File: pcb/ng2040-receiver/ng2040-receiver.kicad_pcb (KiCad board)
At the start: 2 copper layers, 40 x 37 mm, 16 parts, among them J1 DB15_F, SW1 OPTS, U1 RP2040-Zero, U2 NRF24L01_Breakout

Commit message: WIP moving radio to top of receiver
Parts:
- removed C1: 0.1uF, Capacitor_SMD:C_0805_2012Metric_Pad1.18x1.45mm_HandSolder
- added C3: 0.1uF, Capacitor_SMD:C_0805_2012Metric_Pad1.18x1.45mm_HandSolder, F.Cu at (90.6, 73.6)
- added C4: 10uF, Capacitor_SMD:C_0805_2012Metric_Pad1.18x1.45mm_HandSolder, F.Cu at (88.4, 73.6)
- C2: value 0.1uF -> 10nF; moved to F.Cu
- R1, R10, R2, R3, R4, R5, R6, R7, R8, R9, U1: moved to B.Cu
- U2: moved to F.Cu
- moved U1 19.5 mm to (104.6, 57.7), turned to -90 degrees
- moved C2 19.0 mm to (92.8, 73.6), turned to 90 degrees
- moved U2 13.3 mm to (100.0, 66.8)
- moved R9 10.3 mm to (102.2, 81.0)
- moved SW1 7.29 mm to (115.4, 70.8), turned to -90 degrees
- moved R8 7.01 mm to (99.7, 81.0)
- moved R7 6.62 mm to (97.1, 81.0)
- moved R6 6.23 mm to (94.6, 81.0)
- moved R5 5.84 mm to (92.0, 81.0)
- moved R4 5.45 mm to (89.4, 81.0)
- moved R3 5.06 mm to (86.9, 81.0)
- moved R10 4.83 mm to (104.8, 81.0)
- moved R2 4.68 mm to (84.3, 81.0)
- moved R1 4.29 mm to (81.8, 81.0)
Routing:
- net /STA: track 40.6 -> 12.3 mm
- net /SET_PLAYER: track 25.5 -> 0.00 mm, vias 1 -> 0
- net /SET_POWER: track 23.1 -> 0.00 mm, vias 1 -> 0
- net /BD: track 34.0 -> 11.5 mm
- net /BC: track 34.7 -> 13.9 mm
- net /DU: track 36.5 -> 16.8 mm
- net /BB: track 30.4 -> 10.9 mm
- net /BA: track 32.9 -> 14.2 mm
- net /SEL: track 31.2 -> 13.5 mm
- net /DR: track 29.4 -> 12.0 mm
- net GND: track 16.6 -> 0.00 mm, vias 33 -> 10
- net /DL: track 32.6 -> 16.5 mm
- net /MOSI: track 32.8 -> 17.8 mm, vias 0 -> 1
- net /VCC: track 17.4 -> 32.0 mm, vias 0 -> 1
- net /DD: track 30.3 -> 15.7 mm
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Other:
- board text added: "TODO put NRF on top"

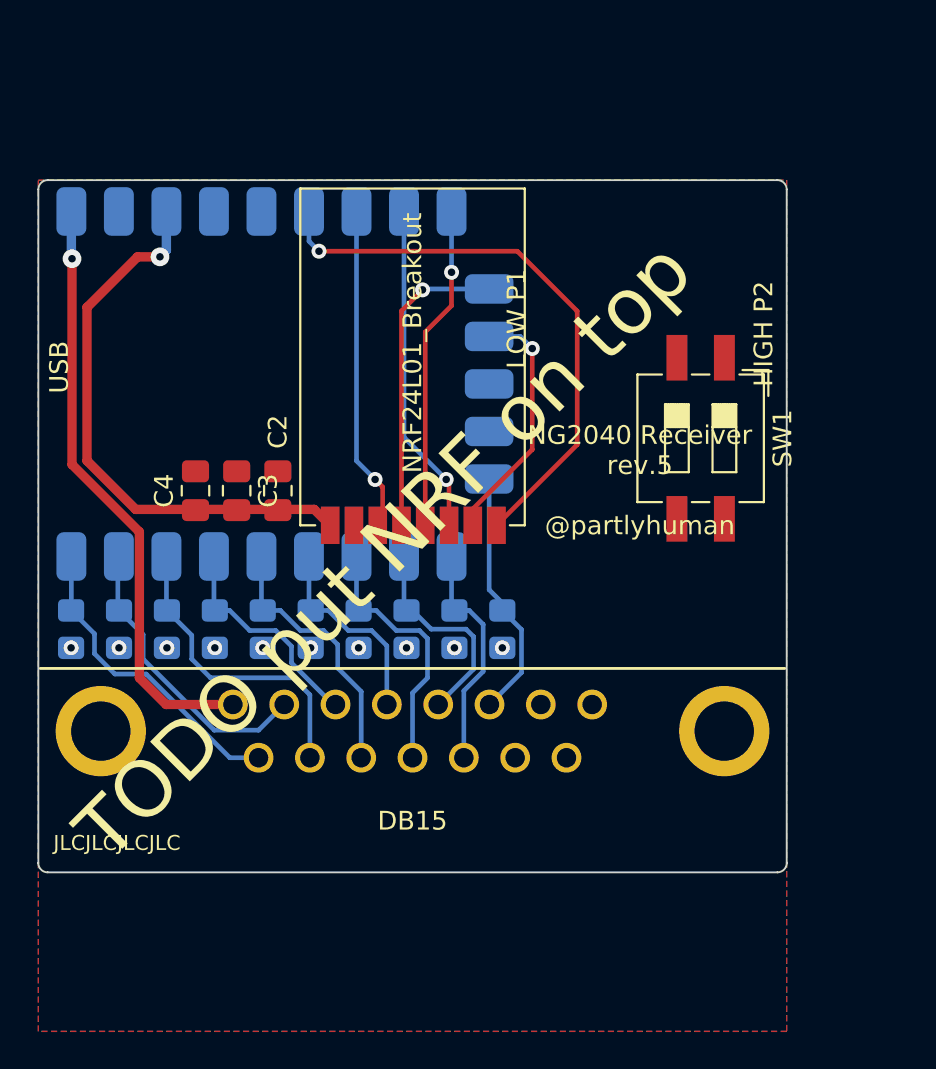
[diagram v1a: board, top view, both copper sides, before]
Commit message: trimming receiver board
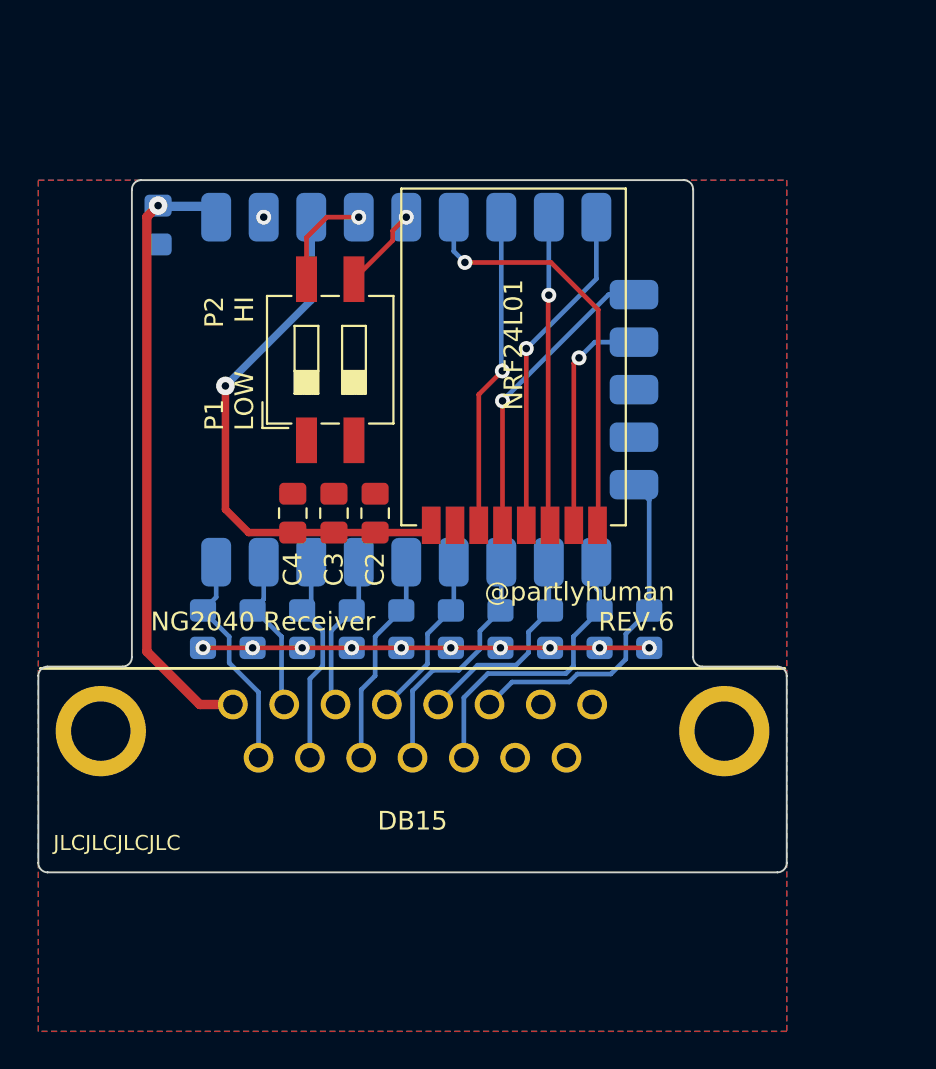
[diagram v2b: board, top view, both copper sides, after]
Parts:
- added C1: 0.1uF, Capacitor_SMD:C_0805_2012Metric_Pad1.18x1.45mm_HandSolder, B.Cu at (86.4, 59.4)
- U2: value NRF24L01_Breakout -> NRF24L01
- moved SW1 20.2 mm to (95.6, 66.6), turned to 90 degrees
- moved R10 7.85 mm to (112.7, 81.0)
- moved R9 7.76 mm to (110.0, 81.0)
- moved U1 7.75 mm to (112.4, 58.0)
- moved R8 7.67 mm to (107.3, 81.0)
- moved R7 7.58 mm to (104.7, 81.0)
- moved R6 7.49 mm to (102.0, 81.0)
- moved R5 7.41 mm to (99.4, 81.0)
- moved R4 7.32 mm to (96.8, 81.0)
- moved R3 7.23 mm to (94.1, 81.0)
- moved R2 7.14 mm to (91.5, 81.0)
- moved R1 7.05 mm to (88.8, 81.0)
- moved U2 5.40 mm to (105.4, 66.8)
- moved C2 5.34 mm to (98.0, 74.8)
- moved C3 5.34 mm to (95.8, 74.8)
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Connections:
- SW1 pad 1: /SET_PLAYER -> GND
- SW1 pad 2: /SET_POWER -> GND
- SW1 pad 3: GND -> /SET_POWER
- SW1 pad 4: GND -> /SET_PLAYER
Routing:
- net GND: track 0.00 -> 23.9 mm, vias 10 -> 11
- net /IRQ: track 30.7 -> 22.4 mm
- net /DD: track 15.7 -> 8.64 mm
- net /SET_PLAYER: track 0.00 -> 5.47 mm, vias 0 -> 1
- net /DL: track 16.5 -> 11.4 mm
- net /SEL: track 13.5 -> 18.5 mm
- net /DU: track 16.8 -> 12.0 mm
- net /SET_POWER: track 0.00 -> 4.47 mm, vias 0 -> 1
- net /DR: track 12.0 -> 8.32 mm
- net /STA: track 12.3 -> 16.0 mm
- net /BA: track 14.2 -> 11.5 mm
- net /BB: track 10.9 -> 9.09 mm
- net /MOSI: track 17.8 -> 16.5 mm
- net /VCC: track 32.0 -> 33.2 mm
- net /3V3: track 30.2 -> 29.2 mm
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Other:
- outline, holes or cut-outs redrawn
- board text added: "${COMPANY} REV.${REVISION}"
- board text added: "${TITLE}"
- board text added: "P1 LOW"
- board text added: "P2 HI"
- board text removed: "${TITLE} rev.${REVISION} ${COMPANY}"
- board text removed: "HIGH P2"
- board text removed: "LOW P1"
- board text removed: "TODO put NRF on top"

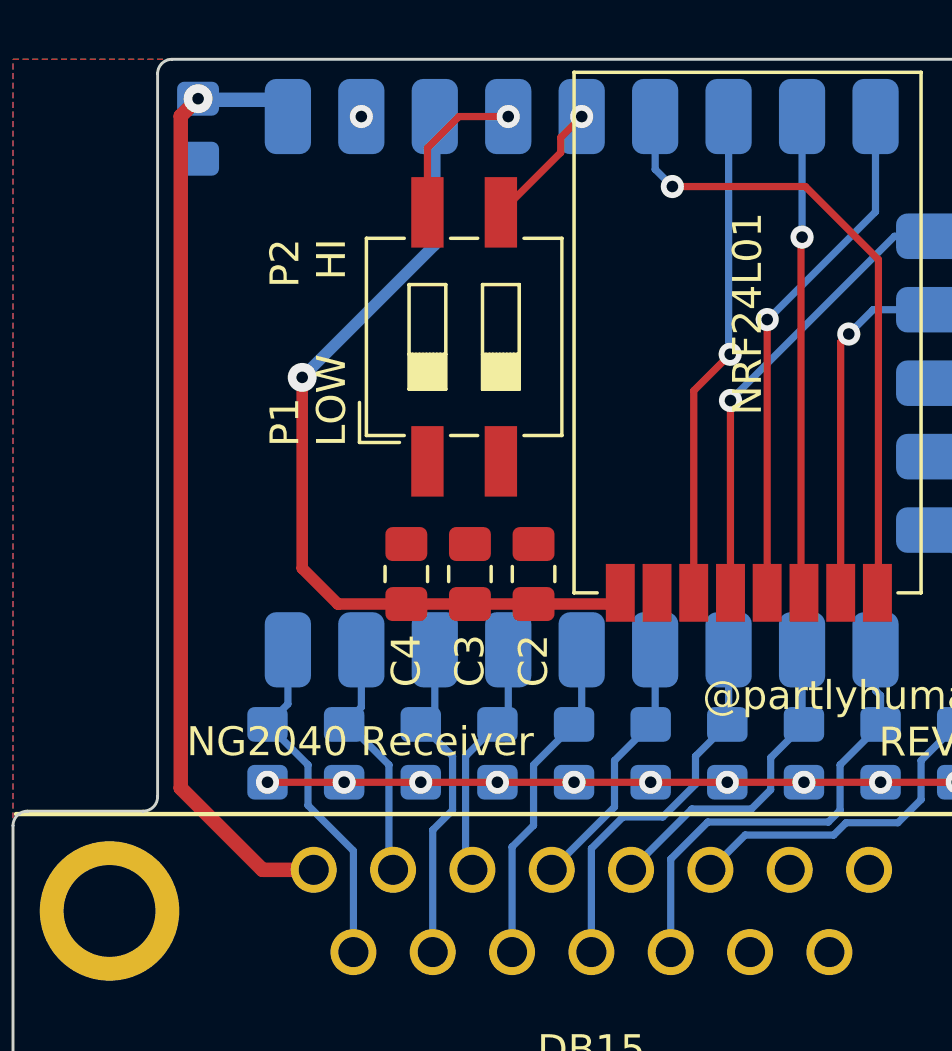
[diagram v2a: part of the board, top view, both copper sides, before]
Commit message: Rerouting
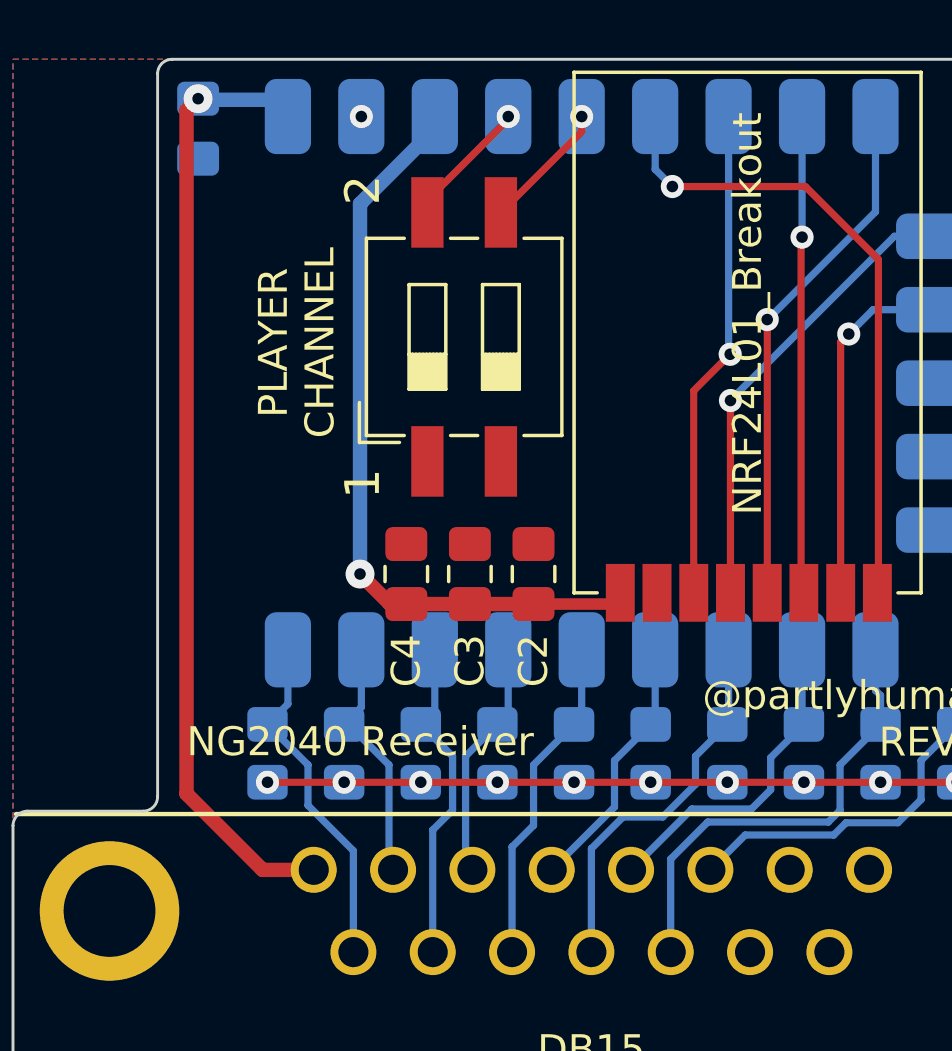
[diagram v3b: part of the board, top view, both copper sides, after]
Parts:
- U2: value NRF24L01 -> NRF24L01_Breakout
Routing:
- net /3V3: track 29.2 -> 26.5 mm
- net /SET_PLAYER: track 5.47 -> 4.47 mm
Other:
- board text added: "1"
- board text added: "2"
- board text added: "PLAYER CHANNEL"
- board text removed: "P1 LOW"
- board text removed: "P2 HI"
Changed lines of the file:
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@@
 			)
 		)
-		(property "Value" "NRF24L01"
+		(property "Value" "NRF24L01_Breakout"
 			(at 0 -0.95 90)
 			(unlocked yes)
@@
 		)
 		(fp_text user "${REFERENCE}"
-			(at 2.579999 0 360)
+			(at 2.579999 0 0)
 			(layer "F.Fab")
 			(effects
@@
 		)
 	)
-	(gr_text "P2\nHI"
-		(at 91.6 63.2 90)
+	(gr_text "2"
+		(at 92.8 61 90)
 		(layer "F.SilkS")
 		(effects
 			(font
-				(size 1 1)
+				(size 1.2 1.2)
 				(thickness 0.15)
 			)
@@
 		)
 	)
-	(gr_text "P1\nLOW"
-		(at 91.6 70.4 90)
+	(gr_text "1"
+		(at 92.8 72.2 90)
 		(layer "F.SilkS")
 		(effects
 			(font
-				(size 1 1)
+				(size 1.2 1.2)
 				(thickness 0.15)
 			)
@@
 		)
 	)
+	(gr_text "PLAYER\nCHANNEL"
+		(at 91.2 66.8 90)
+		(layer "F.SilkS")
+		(effects
+			(font
+				(size 1 1)
+				(thickness 0.15)
+			)
+			(justify bottom)
+		)
+	)
 	(gr_text "${COMPANY}\nREV.${REVISION}"
 		(at 114 81.2 0)
@@
 	)
 	(segment
-		(start 85.8 82.2)
-		(end 88.6284 85.0284)
+		(start 86.4 58.3625)
+		(end 86 58.7625)
 		(width 0.5)
 		(layer "F.Cu")
@@
 	)
 	(segment
-		(start 86.4 58.3625)
-		(end 85.8 58.9625)
+		(start 86 58.7625)
+		(end 86 82.4)
 		(width 0.5)
 		(layer "F.Cu")
@@
 	)
 	(segment
-		(start 88.6284 85.0284)
-		(end 90.398799 85.0284)
+		(start 86 82.4)
+		(end 88.6284 85.0284)
 		(width 0.5)
 		(layer "F.Cu")
@@
 	)
 	(segment
-		(start 85.8 58.9625)
-		(end 85.8 82.2)
+		(start 88.6284 85.0284)
+		(end 90.398799 85.0284)
 		(width 0.5)
 		(layer "F.Cu")
@@
 	)
 	(segment
-		(start 90 68)
-		(end 90 74.6)
-		(width 0.4)
-		(layer "F.Cu")
-		(net 21)
-	)
-	(segment
-		(start 90 74.6)
-		(end 91.2375 75.8375)
+		(start 98 75.8375)
+		(end 100.6125 75.8375)
 		(width 0.4)
 		(layer "F.Cu")
@@
 	)
 	(segment
-		(start 98 75.8375)
-		(end 100.6125 75.8375)
+		(start 100.6125 75.8375)
+		(end 101 75.45)
 		(width 0.4)
 		(layer "F.Cu")
@@
 	)
 	(segment
-		(start 91.2375 75.8375)
+		(start 93.0375 75.8375)
 		(end 98 75.8375)
-		(width 0.4)
+		(width 0.5)
 		(layer "F.Cu")
 		(net 21)
 	)
 	(segment
-		(start 100.6125 75.8375)
-		(end 101 75.45)
-		(width 0.4)
+		(start 92 74.8)
+		(end 93.0375 75.8375)
+		(width 0.5)
 		(layer "F.Cu")
 		(net 21)
 	)
 	(via
-		(at 90 68)
+		(at 92 74.8)
 		(size 1)
 		(drill 0.4)
@@
 	)
 	(segment
-		(start 90 68)
-		(end 94.585 63.415)
-		(width 0.4)
+		(start 92 74.8)
+		(end 92 62)
+		(width 0.5)
 		(layer "B.Cu")
 		(net 21)
 	)
 	(segment
-		(start 94.585 63.415)
+		(start 94.585 59.415)
 		(end 94.585 58.98)
-		(width 0.4)
+		(width 0.5)
+		(layer "B.Cu")
+		(net 21)
+	)
+	(segment
+		(start 92 62)
+		(end 94.585 59.415)
+		(width 0.5)
 		(layer "B.Cu")
 		(net 21)
@@
 	)
 	(segment
-		(start 98.94 59.705)
-		(end 98.94 60.225)
+		(start 99.665 59.5)
+		(end 96.87 62.295)
 		(width 0.25)
 		(layer "F.Cu")
@@
 	(segment
 		(start 99.665 58.98)
-		(end 98.94 59.705)
-		(width 0.25)
-		(layer "F.Cu")
-		(net 23)
-	)
-	(segment
-		(start 98.94 60.225)
-		(end 96.87 62.295)
+		(end 99.665 59.5)
 		(width 0.25)
 		(layer "F.Cu")
@@
 	)
 	(segment
-		(start 94.33 60.07)
-		(end 94.33 62.295)
+		(start 97.125 59.075)
+		(end 94.33 61.87)
 		(width 0.25)
 		(layer "F.Cu")
@@
 	)
 	(segment
-		(start 97.125 58.98)
-		(end 95.42 58.98)
+		(start 94.33 61.87)
+		(end 94.33 62.295)
 		(width 0.25)
 		(layer "F.Cu")
@@
 	)
 	(segment
-		(start 95.42 58.98)
-		(end 94.33 60.07)
+		(start 97.125 58.98)
+		(end 97.125 59.075)
 		(width 0.25)
 		(layer "F.Cu")

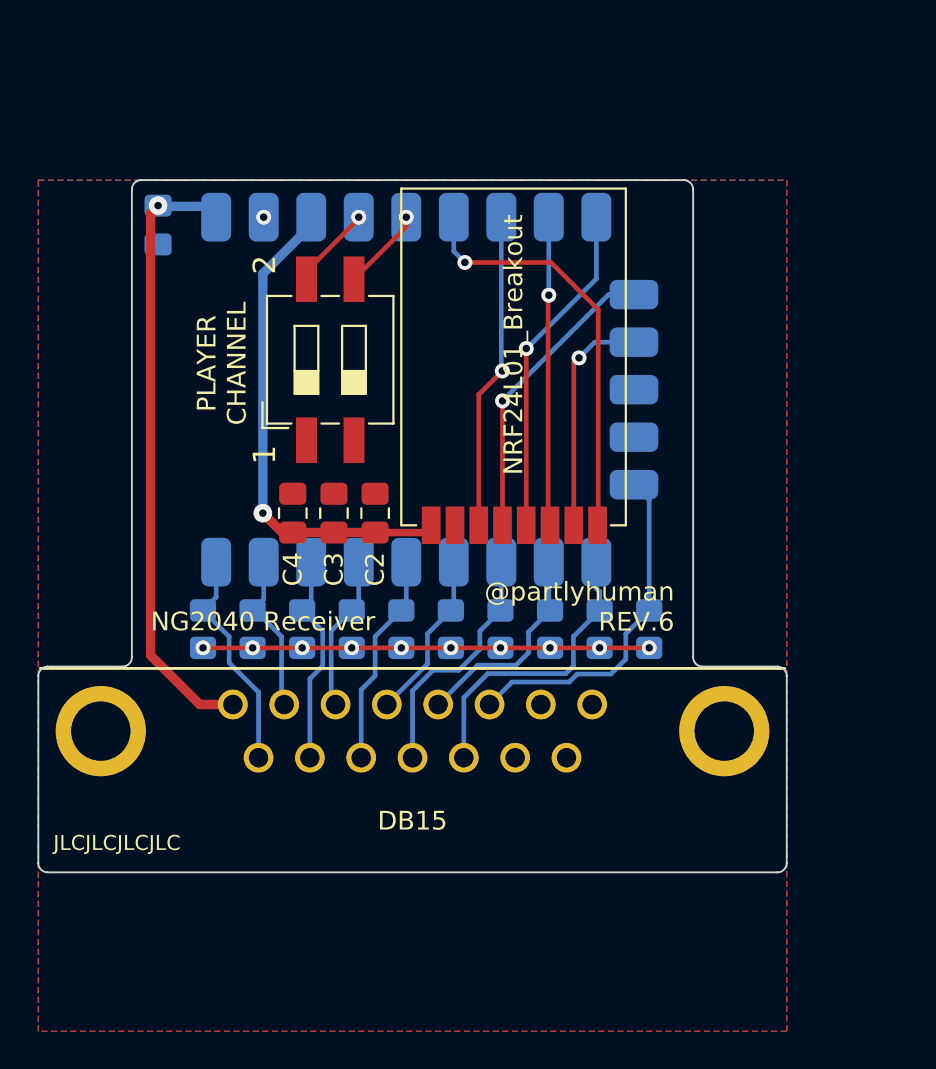
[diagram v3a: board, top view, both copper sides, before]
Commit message: Centers radio on receiver and increments to rev7
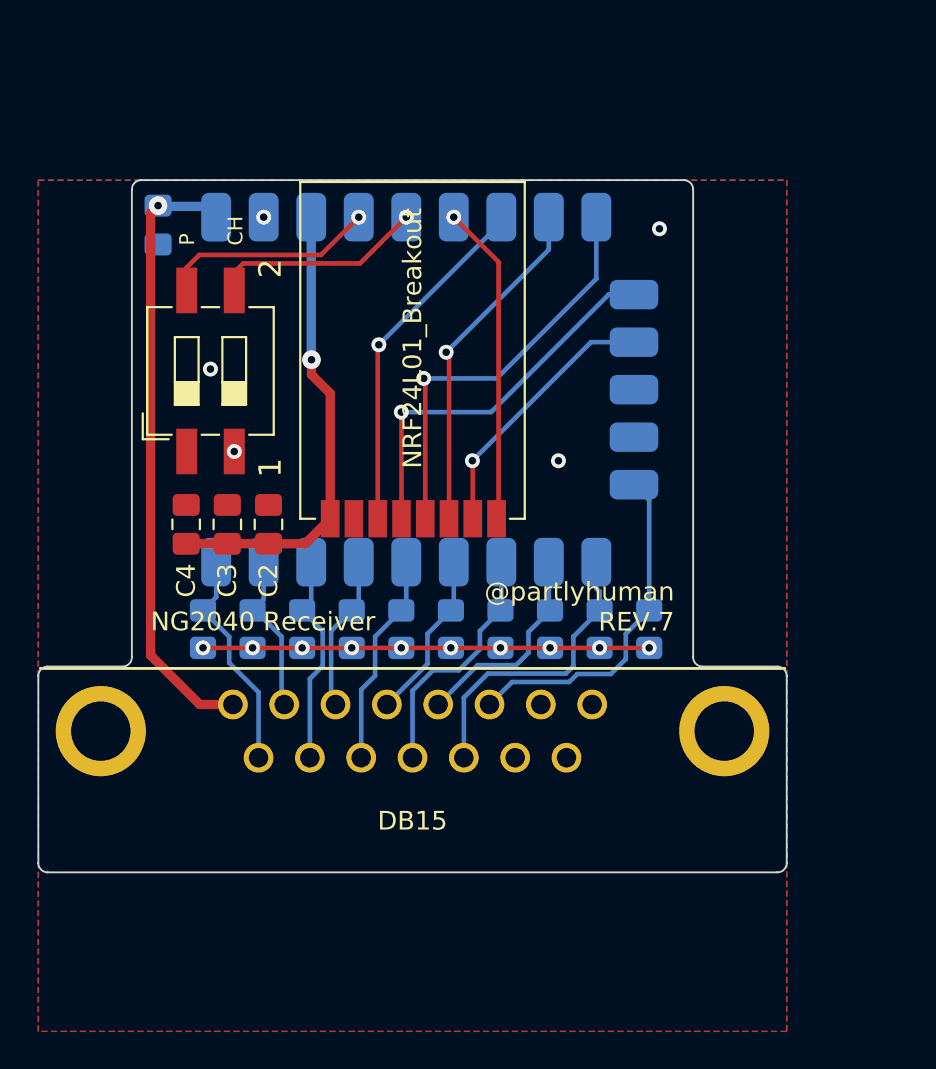
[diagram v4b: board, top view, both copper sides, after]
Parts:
- moved SW1 6.43 mm to (89.2, 67.2)
- moved C2 5.73 mm to (92.3, 75.4)
- moved C3 5.73 mm to (90.1, 75.4)
- moved C4 5.73 mm to (87.9, 75.4)
- moved U2 5.41 mm to (100.0, 66.4)
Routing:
- net /SET_PLAYER: track 4.47 -> 11.5 mm
- net /SET_POWER: track 4.47 -> 11.4 mm
- net /IRQ: track 22.4 -> 17.2 mm
- net /CS: track 16.0 -> 20.7 mm
- net /SCK: track 18.0 -> 22.3 mm
- net /MISO: track 12.3 -> 14.4 mm
- net /MOSI: track 16.5 -> 18.5 mm
- net /CE: track 17.0 -> 18.9 mm
- net /3V3: track 26.5 -> 24.9 mm
- net GND: vias 11 -> 15
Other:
- board text added: "P CH"
- board text removed: "JLCJLCJLCJLC"
- board text removed: "PLAYER CHANNEL"
